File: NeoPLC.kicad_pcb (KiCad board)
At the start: 2 copper layers, 75 x 110 mm, 39 parts, among them J1 Backplane 2x6, J2 DI1-4+COM 3.5mm, J3 DI5-8+COM 3.5mm, J4 SWD, U1 STM32G071CBT6, U2 AP2112K-3.3, U3 ISL3178EIBZ, U4 TLP291-4, U5 TLP291-4, Y1 8MHz

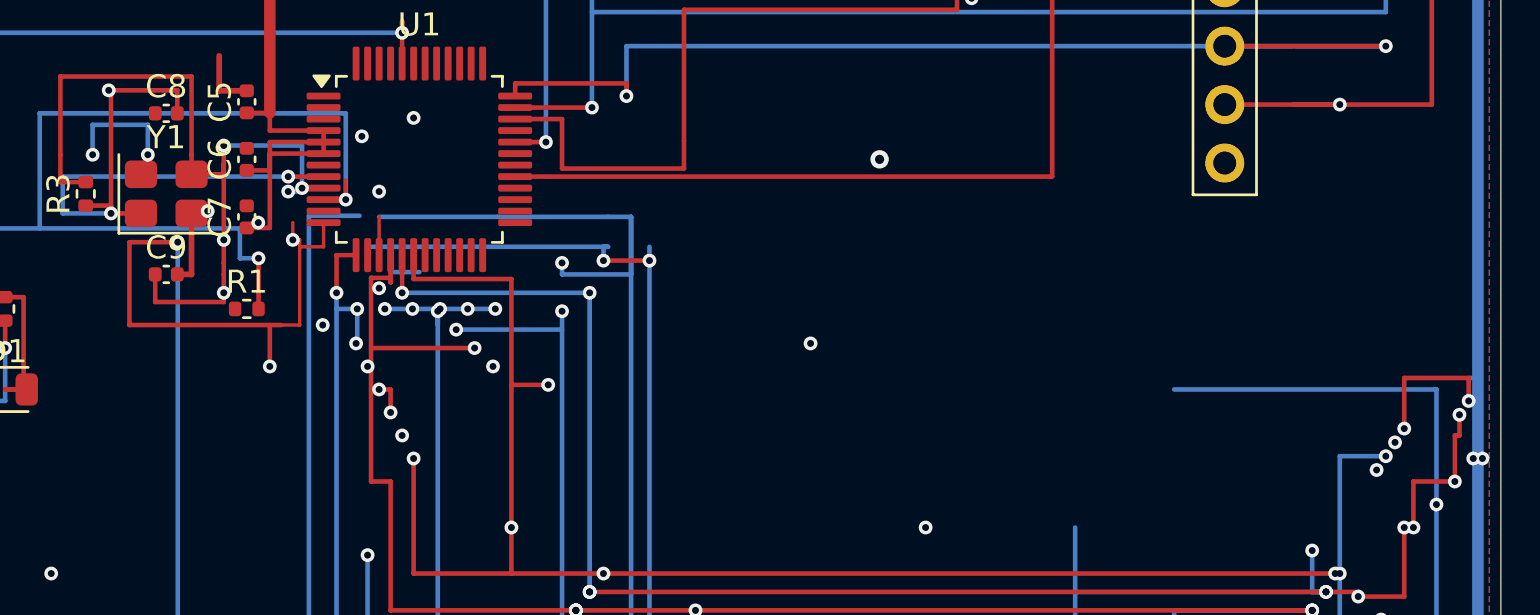
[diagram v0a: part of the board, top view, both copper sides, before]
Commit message: DI3/5/6/7 MCU–saha kapandı, ada via’lar silindi: DRC 54→43, kısa yok.
Co-authored-by: Cursor <cursoragent@cursor.com>
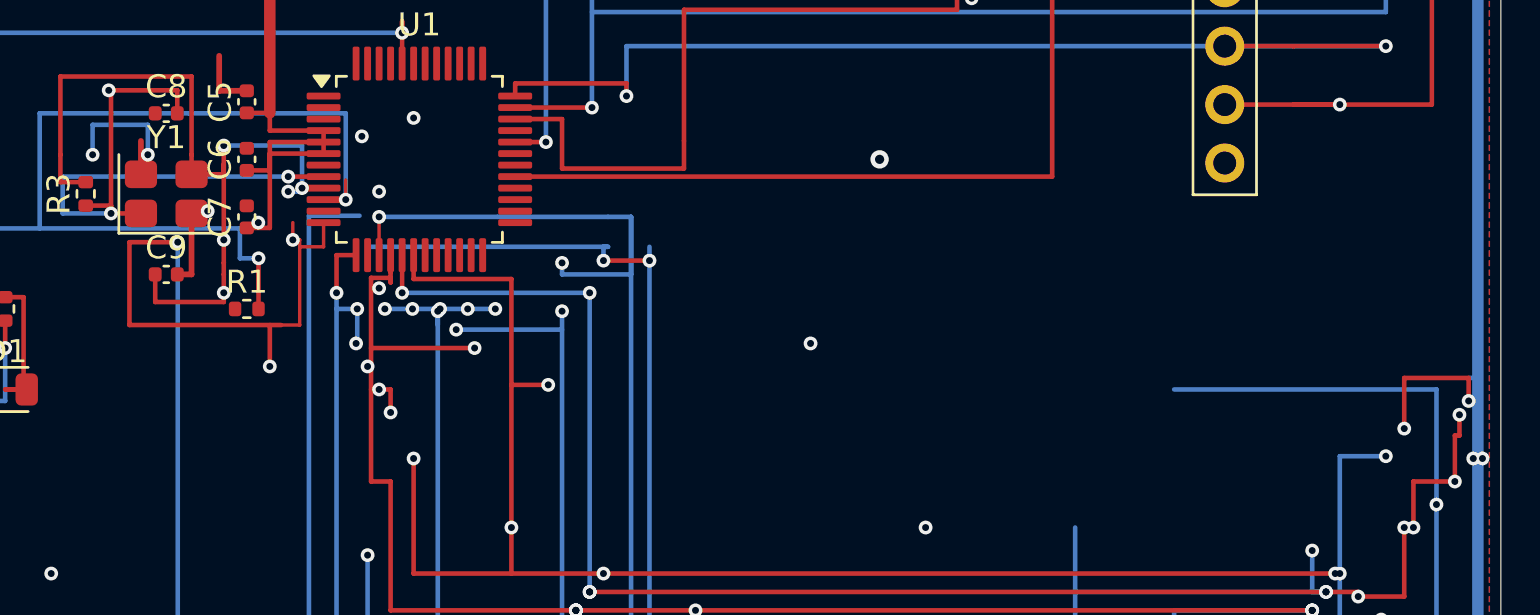
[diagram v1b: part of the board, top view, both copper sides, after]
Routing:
- net GND: track 81.4 -> 82.8 mm
- net /DI Field/DI6: track 109.4 -> 108.9 mm
- net /DI Field/DI7: vias 19 -> 17
- net /DI Field/DI4: vias 16 -> 15
- net /DI Field/DI3: vias 8 -> 7
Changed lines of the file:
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@@
+	)
+	(segment
+		(start 15.9 32.65)
+		(end 15.9 31.2)
+		(width 0.25)
+		(layer "F.Cu")
+		(net "GND")
 	)
 	(segment
@@
 	)
 	(via
-		(at 69.6 45.5)
-		(size 0.6)
-		(drill 0.3)
-		(layers "F.Cu" "B.Cu")
-		(net "/DI Field/DI3")
-	)
-	(via
 		(at 18 67.8)
 		(size 0.6)
@@
 	)
 	(via
-		(at 31.2 41)
-		(size 0.6)
-		(drill 0.3)
-		(layers "F.Cu" "B.Cu")
-		(net "/DI Field/DI7")
-	)
-	(via
 		(at 35.4 37.8)
 		(size 0.6)
@@
 	(via
 		(at 71.2 48)
-		(size 0.6)
-		(drill 0.3)
-		(layers "F.Cu" "B.Cu")
-		(net "/DI Field/DI7")
-	)
-	(via
-		(at 27.25 44)
 		(size 0.6)
 		(drill 0.3)
@@
 	)
 	(segment
+		(start 26.75 36.1625)
+		(end 26.75 36.9)
+		(width 0.2)
+		(layer "F.Cu")
+		(net "/DI Field/DI6")
+	)
+	(segment
 		(start 60.01 62.4)
 		(end 60.01 60)
@@
 		(start 60.8 54.3)
 		(end 60.8 51.6)
-		(width 0.2)
-		(layer "B.Cu")
-		(net "/DI Field/DI6")
-	)
-	(segment
-		(start 28 36.9)
-		(end 26.75 36.9)
 		(width 0.2)
 		(layer "B.Cu")
@@
 	)
 	(via
-		(at 70.4 44.3)
-		(size 0.6)
-		(drill 0.3)
-		(layers "F.Cu" "B.Cu")
-		(net "/DI Field/DI5")
-	)
-	(via
 		(at 29.6 39.4)
 		(size 0.6)
@@
 	(via
 		(at 34.2 52.4)
+		(size 0.6)
+		(drill 0.3)
+		(layers "F.Cu" "B.Cu")
+		(net "/DI Field/DI5")
+	)
+	(via
+		(at 26.25 34.5)
 		(size 0.6)
 		(drill 0.3)
@@
 		(size 0.6)
 		(drill 0.3)
-		(layers "F.Cu" "B.Cu")
-		(net "/DI Field/DI4")
-	)
-	(via
-		(at 23.8 39.2)
-		(size 0.6)
-		(drill 0.3)

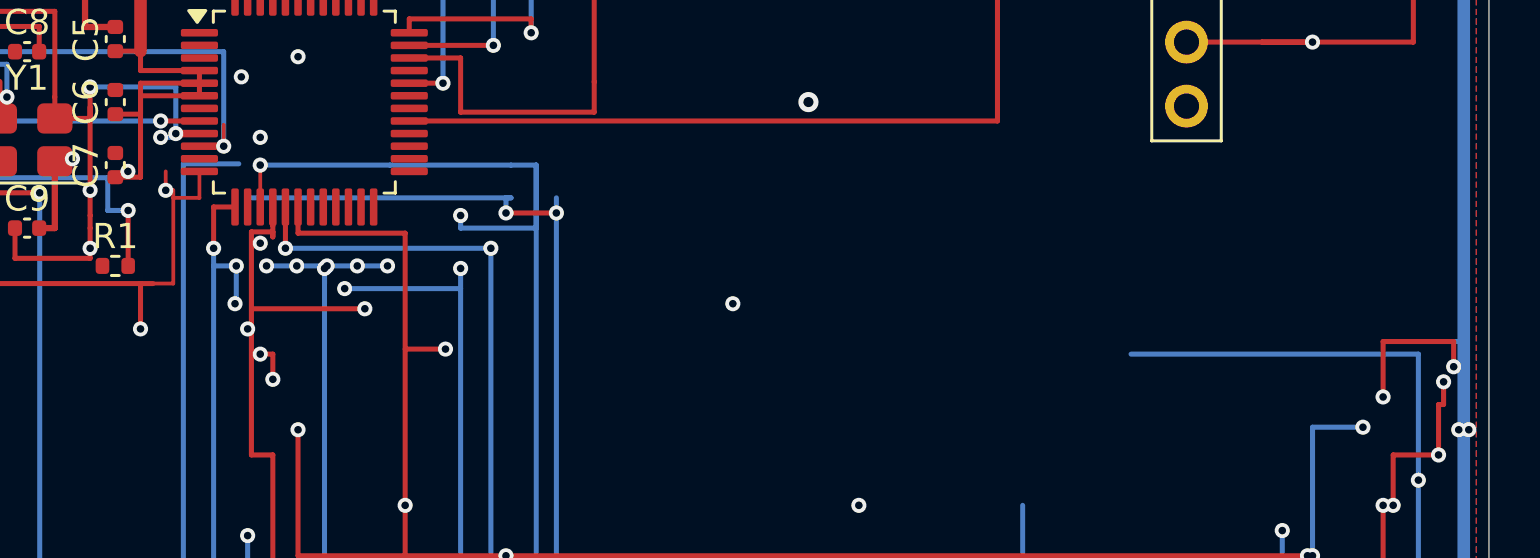
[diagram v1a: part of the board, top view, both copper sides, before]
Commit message: DI1 ve DI4 MCU kaçışı kapandı: 8 DI saha yolu tamam, DRC 43→42, kısa yok.
Co-authored-by: Cursor <cursoragent@cursor.com>
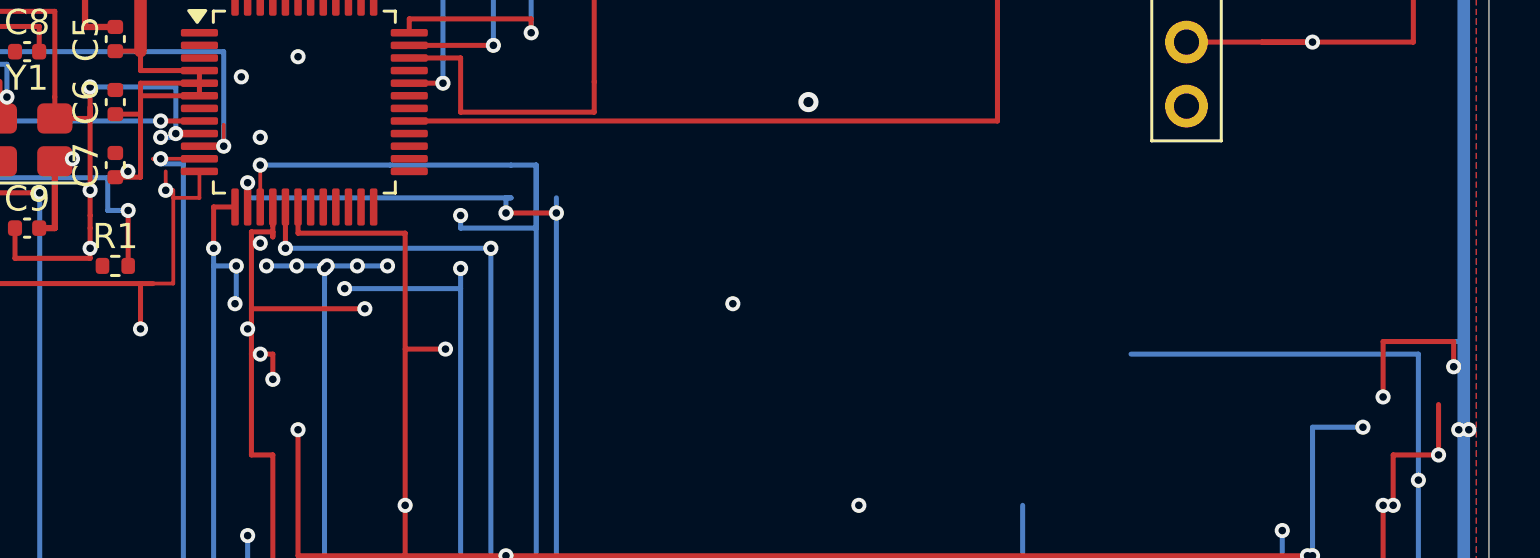
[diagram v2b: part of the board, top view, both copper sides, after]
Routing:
- net /DI Field/DI4: track 100.4 -> 102.0 mm, vias 15 -> 16
- net /DI Field/DI7: track 121.8 -> 120.7 mm, vias 17 -> 16
- net /DI Field/DI1: track 55.5 -> 56.6 mm, vias 5 -> 6
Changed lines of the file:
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@@
-	)
-	(segment
-		(start 73.2 44)
-		(end 73.2 43.1)
-		(width 0.2)
-		(layer "F.Cu")
-		(net "/DI Field/DI7")
 	)
 	(segment
@@
 	)
 	(segment
-		(start 73 44)
-		(end 73.2 44)
-		(width 0.2)
-		(layer "F.Cu")
-		(net "/DI Field/DI7")
-	)
-	(segment
 		(start 68.8 50.8)
 		(end 68.8 51)
@@
 	(via
 		(at 63.5 67.8)
-		(size 0.6)
-		(drill 0.3)
-		(layers "F.Cu" "B.Cu")
-		(net "/DI Field/DI7")
-	)
-	(via
-		(at 73.2 43.1)
 		(size 0.6)
 		(drill 0.3)
@@
 	)
 	(segment
+		(start 22 34.25)
+		(end 22.3 34.25)
+		(width 0.15)
+		(layer "F.Cu")
+		(net "/DI Field/DI1")
+	)
+	(segment
 		(start 12.01 67.8)
 		(end 13 67.8)
@@
 		(net "/DI Field/DI1")
 	)
+	(segment
+		(start 23.8375 34.25)
+		(end 22 34.25)
+		(width 0.15)
+		(layer "F.Cu")
+		(net "/DI Field/DI1")
+	)
 	(via
 		(at 12.01 64)
+		(size 0.6)
+		(drill 0.3)
+		(layers "F.Cu" "B.Cu")
+		(net "/DI Field/DI1")
+	)
+	(via
+		(at 22.3 34.25)
 		(size 0.6)
 		(drill 0.3)
@@
 	)
 	(segment
+		(start 22.3 34.25)
+		(end 22.3 34.45)
+		(width 0.2)
+		(layer "B.Cu")
+		(net "/DI Field/DI1")
+	)
+	(segment
+		(start 22.3 34.45)
+		(end 23.2 34.45)
+		(width 0.2)
+		(layer "B.Cu")
+		(net "/DI Field/DI1")
+	)
+	(segment
 		(start 23.2 59.2)
 		(end 23.2 56)
@@
 	)
 	(segment
-		(start 23.2 34.45)
-		(end 25.4 34.45)
-		(width 0.2)
-		(layer "B.Cu")
-		(net "/DI Field/DI1")
-	)
-	(segment
 		(start 19.5 59.2)
 		(end 23.2 59.2)
@@
 		(net "/DI Field/DI4")
 	)
+	(segment
+		(start 25.75 36.1625)
+		(end 25.75 35.2)
+		(width 0.15)
+		(layer "F.Cu")
+		(net "/DI Field/DI4")
+	)
 	(via
 		(at 36 36.4)
@@
 	(via
 		(at 19.2 62.3)
+		(size 0.6)
+		(drill 0.3)
+		(layers "F.Cu" "B.Cu")
+		(net "/DI Field/DI4")
+	)
+	(via
+		(at 25.75 35.2)
 		(size 0.6)
 		(drill 0.3)
@@
 		(width 0.2)
 		(layer "B.Cu")
+		(net "/DI Field/DI4")
+	)
+	(segment
+		(start 25.75 35.2)
+		(end 25.75 35.8)
+		(width 0.2)
+		(layer "B.Cu")

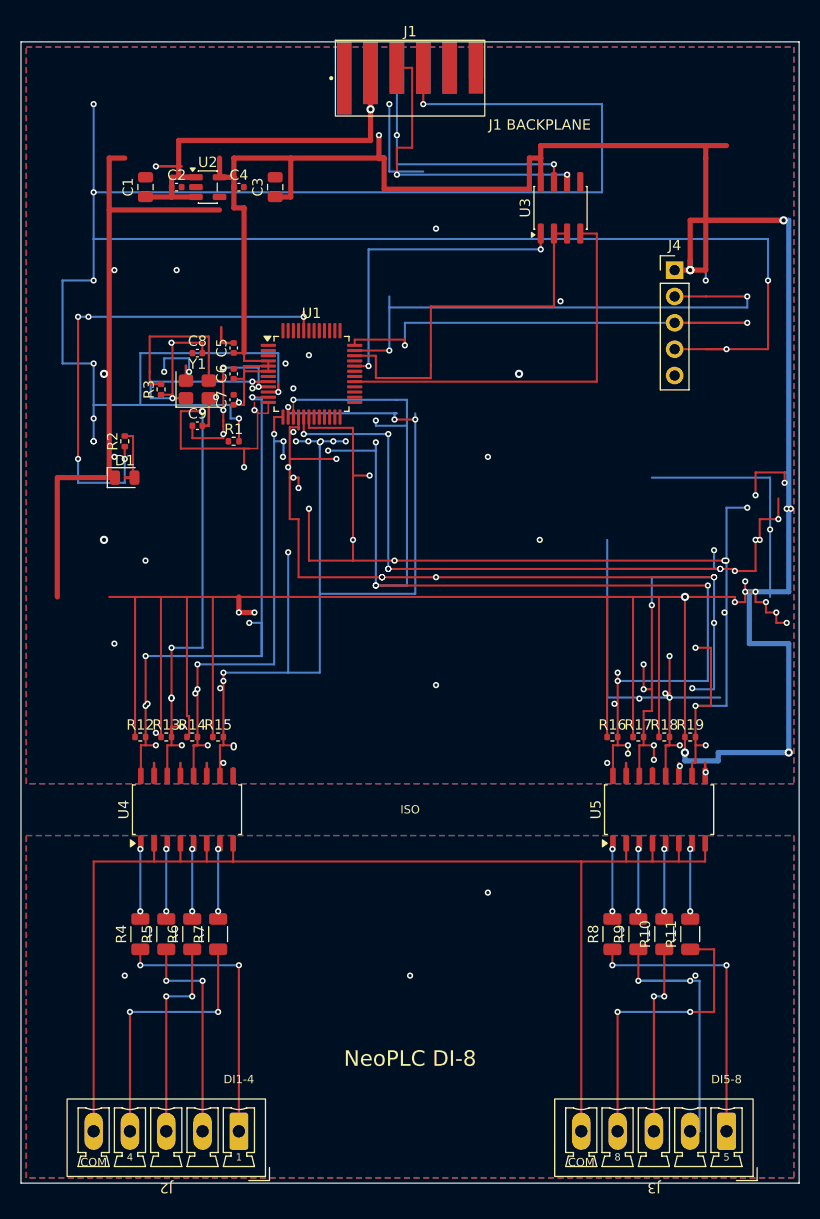
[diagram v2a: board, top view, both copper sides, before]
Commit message: C7, Y1 ve U5 GND dikişi; HSE yığın via silindi: DRC 42→37, kısa yok.
Co-authored-by: Cursor <cursoragent@cursor.com>
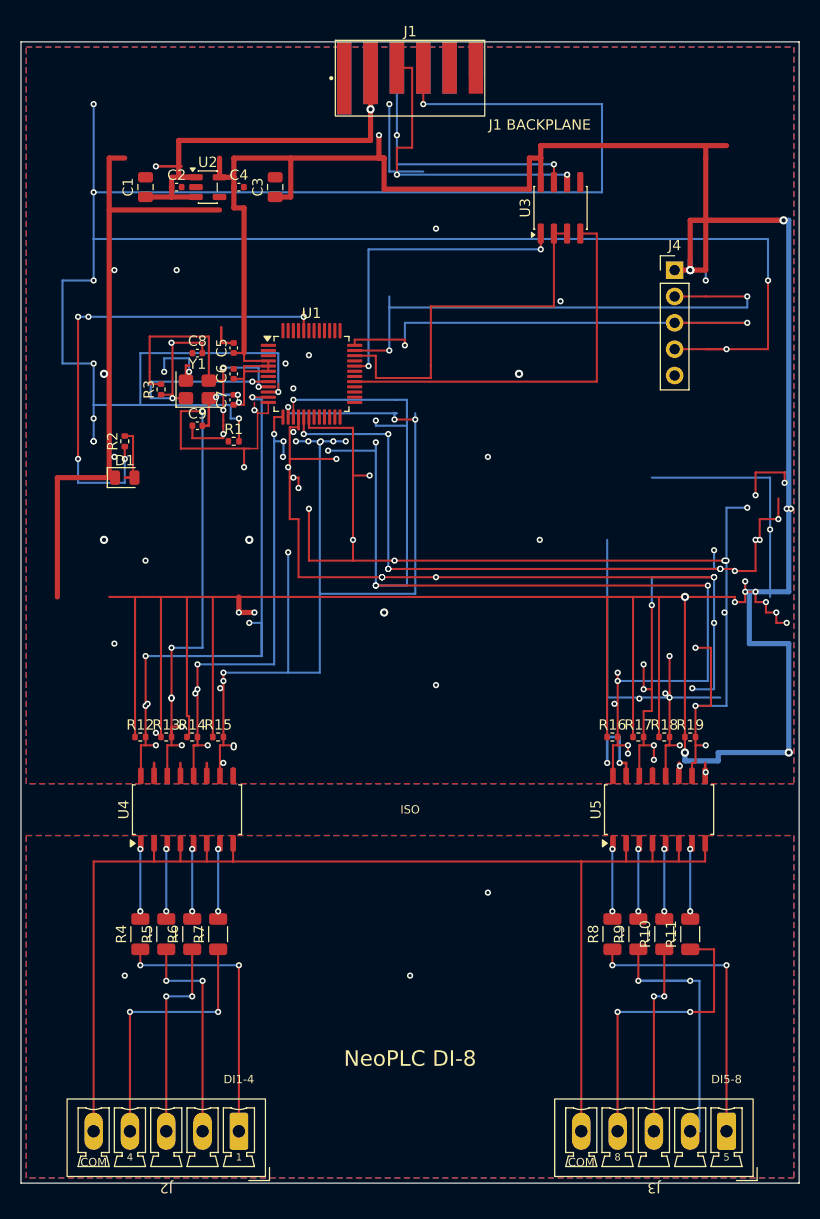
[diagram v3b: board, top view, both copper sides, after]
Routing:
- net GND: track 82.8 -> 93.1 mm, vias 22 -> 26
- net /Node Core/HSE_OUT: track 35.4 -> 34.7 mm, vias 5 -> 4
- net /DI Field/FIELD_COM: vias 4 -> 3
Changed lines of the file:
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@@
+	)
+	(segment
+		(start 15.9 31.2)
+		(end 16.2 31.2)
+		(width 0.25)
+		(layer "F.Cu")
+		(net "GND")
 	)
 	(segment
 		(start 15.9 32.65)
 		(end 15.9 31.2)
+		(width 0.25)
+		(layer "F.Cu")
+		(net "GND")
+	)
+	(segment
+		(start 63.405 69.5)
+		(end 63.5 69.5)
+		(width 0.25)
+		(layer "F.Cu")
+		(net "GND")
+	)
+	(segment
+		(start 20.5 34.02)
+		(end 20.9 34.02)
 		(width 0.25)
 		(layer "F.Cu")
@@
 	)
 	(segment
+		(start 58.325 69.5)
+		(end 57.7 69.5)
+		(width 0.25)
+		(layer "F.Cu")
+		(net "GND")
+	)
+	(segment
 		(start 10 11.2)
 		(end 8.5 11.2)
@@
 	)
 	(segment
+		(start 63.5 69.5)
+		(end 63.5 69.8)
+		(width 0.25)
+		(layer "F.Cu")
+		(net "GND")
+	)
+	(segment
 		(start 20.445 70.75)
 		(end 20.445 70)
@@
 	)
 	(via
+		(at 35 55)
+		(size 0.8)
+		(drill 0.4)
+		(layers "F.Cu" "B.Cu")
+		(net "GND")
+	)
+	(via
 		(at 50 48)
 		(size 0.6)
@@
 	)
 	(via
+		(at 57.7 69.5)
+		(size 0.6)
+		(drill 0.3)
+		(layers "F.Cu" "B.Cu")
+		(net "GND")
+	)
+	(via
 		(at 9 40)
 		(size 0.6)
@@
 	)
 	(via
+		(at 20.9 34.02)
+		(size 0.6)
+		(drill 0.3)
+		(layers "F.Cu" "B.Cu")
+		(net "GND")
+	)
+	(via
 		(at 15 22)
 		(size 0.6)
@@
 	)
 	(via
+		(at 22 48)
+		(size 0.8)
+		(drill 0.4)
+		(layers "F.Cu" "B.Cu")
+		(net "GND")
+	)
+	(via
 		(at 66 70.4)
 		(size 0.6)
@@
 		(drill 0.3)
 		(layers "F.Cu" "B.Cu")
+		(net "GND")
+	)
+	(segment
+		(start 20.9 34.02)
+		(end 18.8 34.02)
+		(width 0.25)
+		(layer "B.Cu")
 		(net "GND")
 	)
@@
 	)
 	(segment
+		(start 57.7 67)
+		(end 56.5 67)
+		(width 0.25)
+		(layer "B.Cu")
+		(net "GND")
+	)
+	(segment
 		(start 13.8 30.5)
 		(end 16.2 30.5)
@@
 	)
 	(segment
+		(start 57.7 69.5)
+		(end 57.7 67)
+		(width 0.25)
+		(layer "B.Cu")
+		(net "GND")
+	)
+	(segment
+		(start 18.8 34.02)
+		(end 18.8 34.25)
+		(width 0.25)
+		(layer "B.Cu")
+		(net "GND")
+	)
+	(segment
+		(start 56.5 67)
+		(end 56.5 69.5)
+		(width 0.25)
+		(layer "B.Cu")
+		(net "GND")
+	)
+	(segment
 		(start 14.6 29)
 		(end 17.48 29)
@@
 	)
 	(via
-		(at 22.3 33.4)
-		(size 0.6)
-		(drill 0.3)
-		(layers "F.Cu" "B.Cu")
-		(net "/Node Core/HSE_OUT")
-	)
-	(via
 		(at 22.9 33.25)
 		(size 0.6)
@@
 		(drill 0.3)
 		(layers "F.Cu" "B.Cu")
-		(net "/Node Core/HSE_OUT")
-	)
-	(segment
-		(start 22.9 33.4)
-		(end 22.9 33.25)
-		(width 0.2)
-		(layer "B.Cu")
 		(net "/Node Core/HSE_OUT")
 	)
@@
 	)
 	(segment
-		(start 22.3 33.4)
-		(end 22.9 33.4)
-		(width 0.2)
-		(layer "B.Cu")
-		(net "/Node Core/HSE_OUT")
-	)
-	(segment
 		(start 10.8 37.99)
 		(end 10.8 42)
@@
 		(size 0.6)
 		(drill 0.3)
-		(layers "F.Cu" "B.Cu")
-		(net "/DI Field/FIELD_COM")
-	)
-	(via
-		(at 65 90)
-		(size 0.6)
-		(drill 0.3)
